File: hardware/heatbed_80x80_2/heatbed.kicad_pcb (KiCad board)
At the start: 2 copper layers, 80 x 80 mm, 1 part, among them J1 PWR

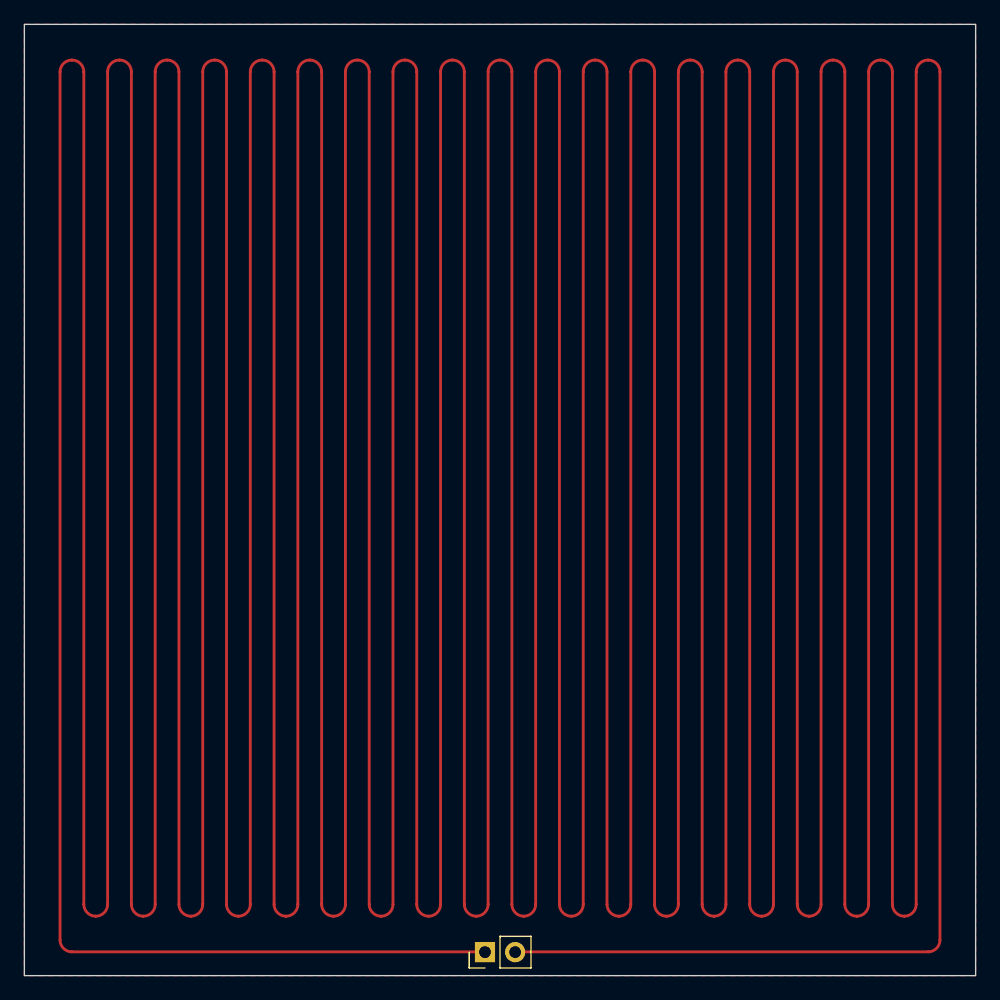
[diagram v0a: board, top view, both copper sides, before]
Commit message: Further increase tracks' widths
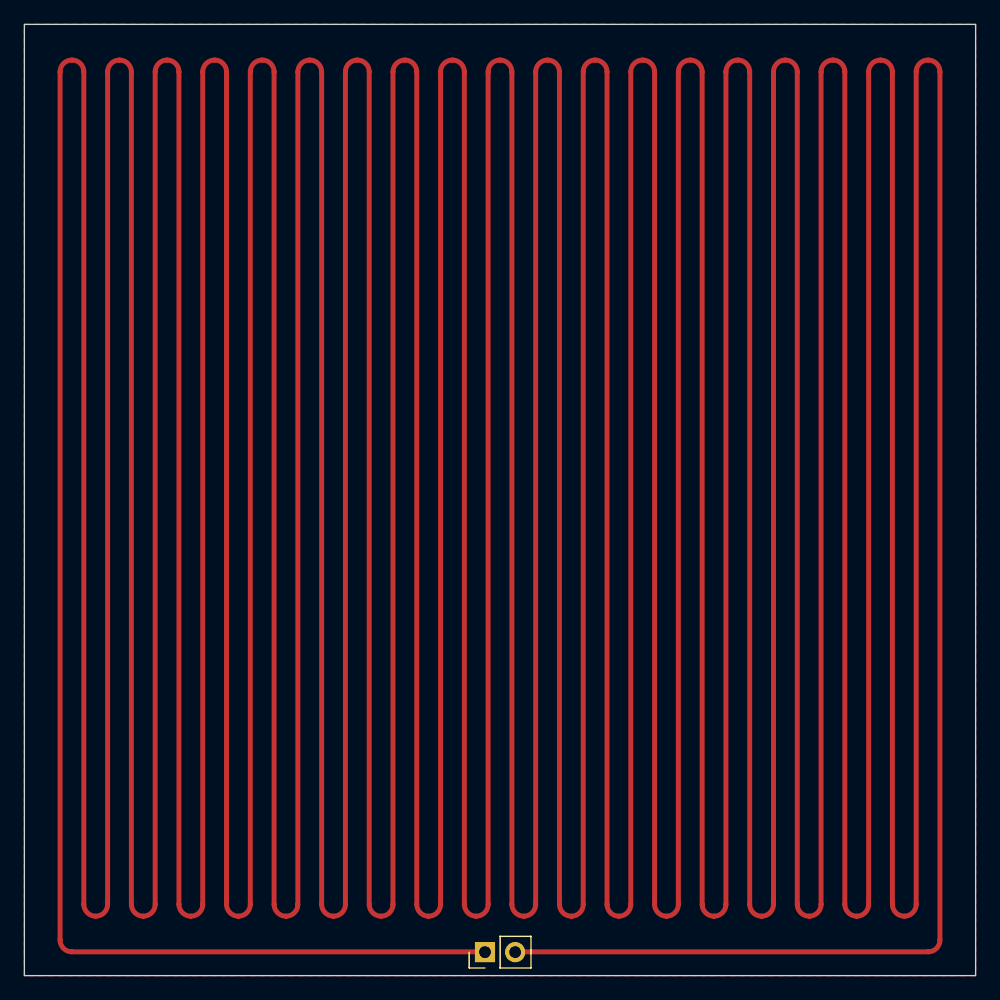
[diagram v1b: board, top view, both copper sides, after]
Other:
- board text added: "Width: 0.418 mm | Length: 2854.91 mm | Resistance: 6.23 Ω"
- board text removed: "Width: 0.241 mm | Length: 2855 mm | Resistance: 9.70 Ω"

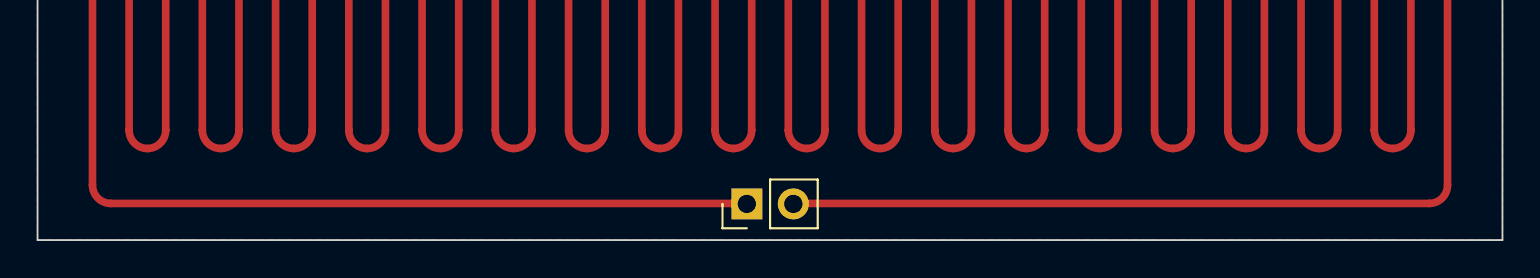
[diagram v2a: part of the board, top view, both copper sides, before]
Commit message: Increase holes' diameters
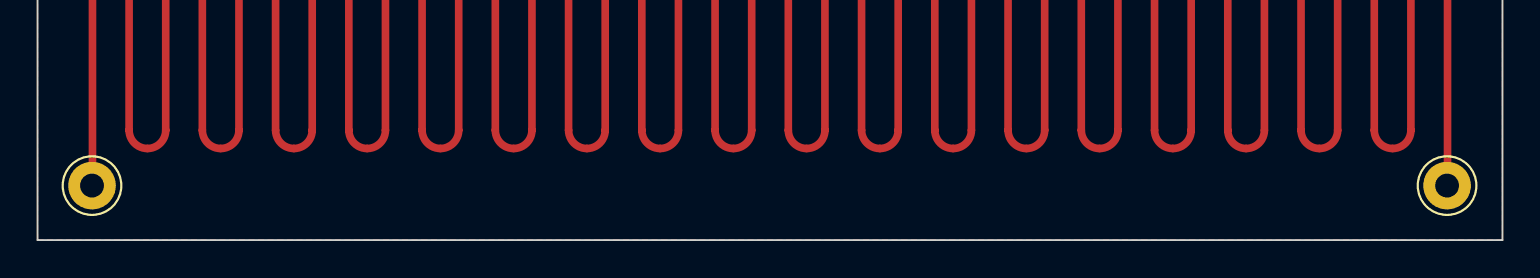
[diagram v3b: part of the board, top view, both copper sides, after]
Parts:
- added J2: Conn_01x01, Connector_Pin:Pin_D1.3mm_L11.0mm, F.Cu at (184.0, 145.0)
- J1: value PWR -> Conn_01x01; footprint Connector_PinHeader_2.54mm:PinHeader_1x02_P2.54mm_Vertical -> Connector_Pin:Pin_D1.3mm_L11.0mm
- moved J1 35.8 mm to (110.0, 145.0), turned to 0 degrees
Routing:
- net Net-(J1-Pin_1): track 2851.8 -> 2779.3 mm
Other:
- board text removed: "Width: 0.418 mm | Length: 2854.91 mm | Resistance: 6.23 Ω"
